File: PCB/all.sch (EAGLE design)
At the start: 41 parts, among them J1 ISP Programmer, U1 ATMEGA32U4, U2 3.3V_REG, U3 MPU-6050-1, U5 MCP73831, U6 AL8805, X1 USBSMD

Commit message: Still playing with GIT - this time I wanted to see how does it recognize the changes in Eagle files.
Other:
- note added: "Tie AD0 somewhere! (to pin 8 is the best) Otherwise, the chip won't work!"
- note removed: "Tie AD0 somewhere! (to pin 8 is the best)"
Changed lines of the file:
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@@
 <?xml version="1.0" encoding="utf-8"?>
 <!DOCTYPE eagle SYSTEM "eagle.dtd">
-<eagle version="7.4.0">
+<eagle version="7.3.0">
 <drawing>
 <settings>
@@
 <text x="179.324" y="-13.716" size="3.81" layer="91">for 3.3V, XTAL
 should be max 8MHz!!!</text>
-<text x="355.6" y="-55.88" size="1.778" layer="91">Tie AD0 somewhere!
-(to pin 8 is the best)</text>
+<text x="353.06" y="-60.96" size="1.778" layer="91">Tie AD0 somewhere!
+(to pin 8 is the best)
+Otherwise, the chip won't work!</text>
 </plain>
 <instances>

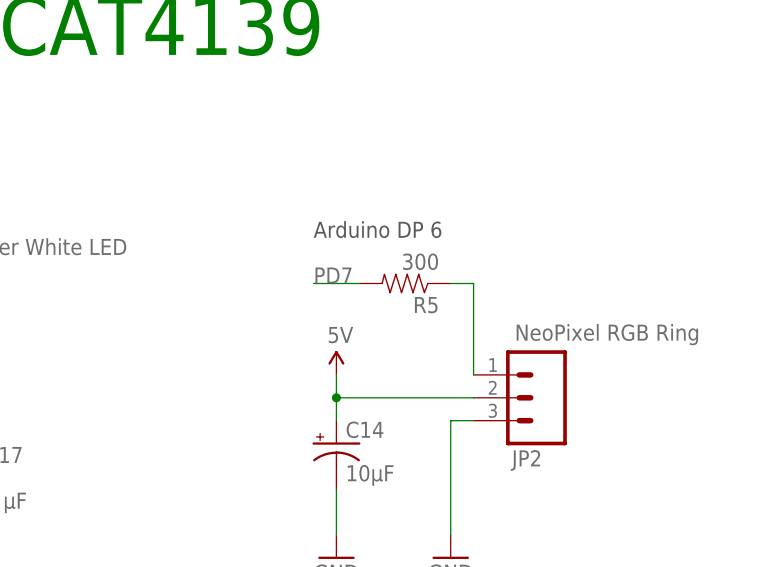
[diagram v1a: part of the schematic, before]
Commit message: added 3D models
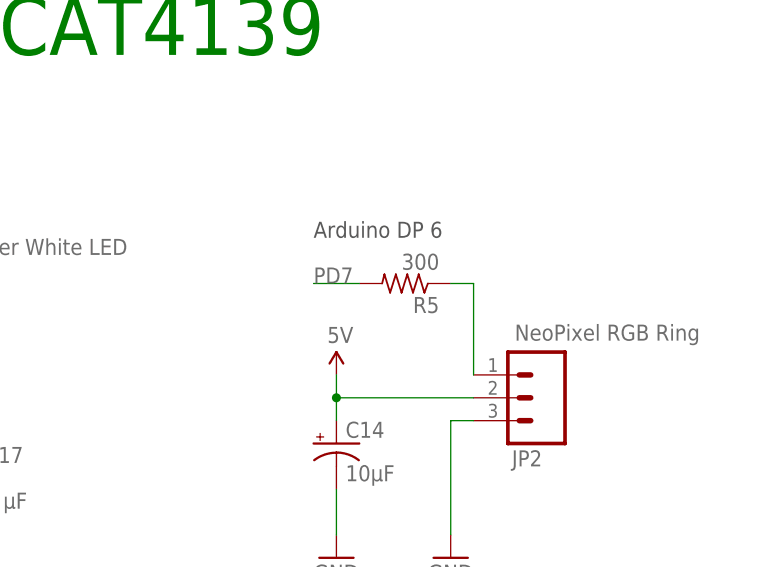
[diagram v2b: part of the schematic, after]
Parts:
- R5: device SparkFun:RESISTOR0603-RES -> rcl:R-US_R0603
- U1: device SparkFun:ATMEGA32U4QFN2 -> SparkFun-Retired:ATMEGA32U4QFN2
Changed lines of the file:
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@@
 <layers>
 <layer number="1" name="Top" color="4" fill="1" visible="no" active="no"/>
+<layer number="2" name="Route2" color="1" fill="3" visible="no" active="no"/>
+<layer number="3" name="Route3" color="4" fill="3" visible="no" active="no"/>
+<layer number="4" name="Route4" color="1" fill="4" visible="no" active="no"/>
+<layer number="5" name="Route5" color="4" fill="4" visible="no" active="no"/>
+<layer number="6" name="Route6" color="1" fill="8" visible="no" active="no"/>
+<layer number="7" name="Route7" color="4" fill="8" visible="no" active="no"/>
+<layer number="8" name="Route8" color="1" fill="2" visible="no" active="no"/>
+<layer number="9" name="Route9" color="4" fill="2" visible="no" active="no"/>
+<layer number="10" name="Route10" color="1" fill="7" visible="no" active="no"/>
+<layer number="11" name="Route11" color="4" fill="7" visible="no" active="no"/>
+<layer number="12" name="Route12" color="1" fill="5" visible="no" active="no"/>
+<layer number="13" name="Route13" color="4" fill="5" visible="no" active="no"/>
+<layer number="14" name="Route14" color="1" fill="6" visible="no" active="no"/>
+<layer number="15" name="Route15" color="4" fill="6" visible="no" active="no"/>
 <layer number="16" name="Bottom" color="1" fill="1" visible="no" active="no"/>
 <layer number="17" name="Pads" color="2" fill="1" visible="no" active="no"/>
@@
 <layer number="54" name="bGND_GNDA" color="1" fill="9" visible="no" active="no"/>
 <layer number="56" name="wert" color="7" fill="1" visible="no" active="no"/>
+<layer number="57" name="tCAD" color="7" fill="1" visible="no" active="no"/>
+<layer number="59" name="tCarbon" color="7" fill="1" visible="no" active="no"/>
+<layer number="60" name="bCarbon" color="7" fill="1" visible="no" active="no"/>
+<layer number="90" name="Modules" color="5" fill="1" visible="yes" active="yes"/>
 <layer number="91" name="Nets" color="2" fill="1" visible="yes" active="yes"/>
 <layer number="92" name="Busses" color="1" fill="1" visible="yes" active="yes"/>
@@
 <layer number="108" name="tplace-old" color="10" fill="1" visible="yes" active="yes"/>
 <layer number="109" name="ref-old" color="11" fill="1" visible="yes" active="yes"/>
+<layer number="110" name="fp0" color="7" fill="1" visible="no" active="yes"/>
+<layer number="111" name="LPC17xx" color="7" fill="1" visible="no" active="yes"/>
+<layer number="112" name="tSilk" color="7" fill="1" visible="no" active="yes"/>
+<layer number="113" name="IDFDebug" color="4" fill="1" visible="no" active="yes"/>
 <layer number="116" name="Patch_BOT" color="9" fill="4" visible="no" active="yes"/>
 <layer number="121" name="_tsilk" color="7" fill="1" visible="no" active="yes"/>
 <layer number="122" name="_bsilk" color="7" fill="1" visible="no" active="yes"/>
+<layer number="123" name="tTestmark" color="7" fill="1" visible="no" active="yes"/>
+<layer number="124" name="bTestmark" color="7" fill="1" visible="no" active="yes"/>
 <layer number="125" name="_tNames" color="7" fill="1" visible="no" active="yes"/>
+<layer number="126" name="_bNames" color="7" fill="1" visible="no" active="yes"/>
+<layer number="127" name="_tValues" color="7" fill="1" visible="no" active="yes"/>
+<layer number="128" name="_bValues" color="7" fill="1" visible="no" active="yes"/>
+<layer number="129" name="Mask" color="7" fill="1" visible="yes" active="yes"/>
+<layer number="131" name="tAdjust" color="7" fill="1" visible="no" active="yes"/>
+<layer number="132" name="bAdjust" color="7" fill="1" visible="no" active="yes"/>
 <layer number="144" name="Drill_legend" color="7" fill="1" visible="no" active="yes"/>
+<layer number="150" name="Notes" color="7" fill="1" visible="no" active="yes"/>
 <layer number="151" name="HeatSink" color="7" fill="1" visible="no" active="yes"/>
+<layer number="152" name="_bDocu" color="7" fill="1" visible="no" active="yes"/>
+<layer number="153" name="FabDoc1" color="7" fill="1" visible="no" active="yes"/>
+<layer number="154" name="FabDoc2" color="7" fill="1" visible="no" active="yes"/>
+<layer number="155" name="FabDoc3" color="7" fill="1" visible="no" active="yes"/>
 <layer number="199" name="Contour" color="7" fill="1" visible="no" active="yes"/>
 <layer number="200" name="200bmp" color="1" fill="10" visible="no" active="yes"/>
@@
 <layer number="223" name="223bmp" color="24" fill="1" visible="no" active="no"/>
 <layer number="224" name="224bmp" color="25" fill="1" visible="no" active="no"/>
+<layer number="225" name="225bmp" color="7" fill="1" visible="yes" active="yes"/>
+<layer number="226" name="226bmp" color="7" fill="1" visible="yes" active="yes"/>
+<layer number="227" name="227bmp" color="7" fill="1" visible="yes" active="yes"/>
+<layer number="228" name="228bmp" color="7" fill="1" visible="yes" active="yes"/>
+<layer number="229" name="229bmp" color="7" fill="1" visible="yes" active="yes"/>
+<layer number="230" name="230bmp" color="7" fill="1" visible="yes" active="yes"/>
+<layer number="231" name="231bmp" color="7" fill="1" visible="yes" active="yes"/>
+<layer number="248" name="Housing" color="7" fill="1" visible="no" active="yes"/>
+<layer number="249" name="Edge" color="7" fill="1" visible="no" active="yes"/>
 <layer number="250" name="Descript" color="3" fill="1" visible="no" active="no"/>
 <layer number="251" name="SMDround" color="12" fill="11" visible="no" active="no"/>
 <layer number="254" name="cooling" color="7" fill="1" visible="no" active="yes"/>
+<layer number="255" name="routoute" color="7" fill="1" visible="yes" active="yes"/>
 </layers>
 <schematic xreflabel="%F%N/%S.%C%R" xrefpart="/%S.%C%R">
@@
 </classes>
 <parts>
-<part name="U1" library="SparkFun" deviceset="ATMEGA32U4" device="QFN2" value="ATMEGA32U4"/>
+<part name="U1" library="SparkFun-Retired" deviceset="ATMEGA32U4" device="QFN2" value="ATMEGA32U4"/>
 <part name="R1" library="rcl" deviceset="R-US_" device="R0603" value="10k"/>
 <part name="C1" library="rcl" deviceset="C-EU" device="C0402" value="0.1μF"/>
@@
 <part name="U$5" library="SparkFun" deviceset="5V" device=""/>
 <part name="GND24" library="SparkFun" deviceset="GND" device=""/>
-<part name="R5" library="SparkFun" deviceset="RESISTOR" device="0603-RES" value="300"/>
+<part name="R5" library="rcl" deviceset="R-US_" device="R0603" value="300"/>
 <part name="C14" library="SparkFun" deviceset="CAP_POL" device="1206" value="10μF"/>
 <part name="GND21" library="SparkFun" deviceset="GND" device=""/>

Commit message: Adding Qi receiver modules
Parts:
- removed F1: PTCSMD, SparkFun:PTCSMD
- removed XTAL1: 16MHz, SparkFun:CRYSTAL5X3
- added C18, C19, C20, C21, C22, C23, C24, C25, C26, C27, C28, C29: 10μF, SparkFun:CAP_POL1206
- added CP1, CP2, CP3, CP4, CP5, CP6, CP7, CP8, CS, CS10, CS17, CS20, CS27, CS30, CS37, CS7: 18pF, rcl:C-EUC0603
- added CS1, CS11, CS12, CS2, CS21, CS22, CS31, CS32: 10nF, rcl:C-EUC0603
- added CS13, CS15, CS23, CS25, CS3, CS33, CS35, CS5: 0.47μF, rcl:C-EUC0603
- added CS14, CS16, CS24, CS26, CS34, CS36, CS4, CS6: 22nF, rcl:C-EUC0603
- added CS18, CS19, CS28, CS29, CS38, CS39, CS8, CS9: 100nF, rcl:C-EUC0603
- added J3, J4, J5, J6: (no value), SparkFun-Connectors:M02PTH2
- added R10, R11, R14, R17: 10k, rcl:R-EU_R0603
- added R12, R15, R4: 188, rcl:R-EU_R0603
- added R13, R16, R9: 230, rcl:R-EU_R0603
- added U4, U7, U8, U9: BQ51013B_RHL_20, pero_library:BQ51013B_RHL_20
- L1: value 33 μH -> 56uH
- R2: value 22 -> 188; device rcl:R-US_R0603 -> rcl:R-EU_R0603
- R3: value 22 -> 230; device rcl:R-US_R0603 -> rcl:R-EU_R0603
- X1: value USBSMD -> 8MHz; device SparkFun:USBSMD -> pero_library:QUARTZ-CRYSTAL-8MHZQC6CB8.00000F18B23R
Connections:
- removed net D+: R2.1, X1.D+
- removed net D-: R3.1, X1.D-
- new net N$10: CS.1, CS7.1, J3.2
- new net N$11: CP1.1, CP2.1, CS2.1, CS3.1, CS4.1, J3.1, U4.AC2
- new net N$12: CS1.2, U4.BOOT1
- new net N$13: CS2.2, U4.BOOT2
- new net N$14: CS3.2, U4.CLMP2
- new net N$19: CS4.2, U4.COM2
- new net N$20: CS6.2, U4.COM1
- new net N$21: CS5.2, U4.CLMP1
- new net N$22: CS12.2, U7.BOOT2
- new net N$23: C20.+, C21.+, CS9.1, U4.RECT
- new net N$24: R9.2, U4.ILIM
- new net N$25: R4.2, R9.1, U4.FOD
- new net N$26: R10.1, U4.TS-CTRL
- new net N$27: CS13.2, U7.CLMP2
- new net N$28: CS14.2, U7.COM2
- new net N$29: CS16.2, U7.COM1
- new net N$30: CS15.2, U7.CLMP1
- new net N$31: CP3.2, CP4.2, CS10.2, CS11.1, CS15.1, CS16.1, CS17.2, U7.AC1
- new net N$32: C22.+, C23.+, CS19.1, U7.RECT
- new net N$33: R3.2, U7.ILIM
- new net N$34: R2.2, R3.1, U7.FOD
- new net N$35: R11.1, U7.TS-CTRL
- new net N$36: CS20.1, CS27.1, J5.2
- new net N$37: CP5.1, CP6.1, CS22.1, CS23.1, CS24.1, J5.1, U8.AC2
- new net N$38: CS21.2, U8.BOOT1
- new net N$39: CS22.2, U8.BOOT2
- new net N$40: CS23.2, U8.CLMP2
- new net N$41: CS24.2, U8.COM2
- new net N$42: CS26.2, U8.COM1
- new net N$43: CS25.2, U8.CLMP1
- new net N$44: CP5.2, CP6.2, CS20.2, CS21.1, CS25.1, CS26.1, CS27.2, U8.AC1
- new net N$45: C25.+, C26.+, CS29.1, U8.RECT
- new net N$46: R13.2, U8.ILIM
- new net N$47: R12.2, R13.1, U8.FOD
- new net N$48: R14.1, U8.TS-CTRL
- new net N$49: CS30.1, CS37.1, J6.2
- new net N$50: CP7.1, CP8.1, CS32.1, CS33.1, CS34.1, J6.1, U9.AC2
- new net N$51: CS31.2, U9.BOOT1
- new net N$52: CS32.2, U9.BOOT2
- new net N$53: CS33.2, U9.CLMP2
- new net N$54: CS34.2, U9.COM2
- new net N$55: CS36.2, U9.COM1
- new net N$56: CS35.2, U9.CLMP1
- new net N$57: CP7.2, CP8.2, CS30.2, CS31.1, CS35.1, CS36.1, CS37.2, U9.AC1
- new net N$58: C28.+, C29.+, CS39.1, U9.RECT
- new net N$59: R16.2, U9.ILIM
- new net N$60: R15.2, R16.1, U9.FOD
- new net N$61: R17.1, U9.TS-CTRL
- new net N$9: CP1.2, CP2.2, CS.2, CS1.1, CS5.1, CS6.1, CS7.2, U4.AC1
- new net V_QI1: C18.+, CS18.1, U7.OUT
- new net V_QI2: C19.+, CS8.1, U4.OUT
- new net V_QI3: C24.+, CS28.1, U8.OUT
- new net V_QI4: C27.+, CS38.1, U9.OUT
- net GND: now also C18.-, C19.-, C20.-, C21.-, C22.-, C23.-, C24.-, C25.-, C26.-, C27.-, C28.-, C29.-, CS18.2, CS19.2, CS28.2, CS29.2, CS38.2, CS39.2, CS8.2, CS9.2, R10.2, R11.2, R12.1, R14.2, R15.1, R17.2, R2.1, R4.1, U4.AD, U4.EN1, U4.EN2, U4.EPAD, U4.PGND, U4.PGND_2, U7.AD, U7.EN1, U7.EN2, U7.EPAD, U7.PGND, U7.PGND_2, U8.AD, U8.EN1, U8.EN2, U8.EPAD, U8.PGND, U8.PGND_2, U9.AD, U9.EN1, U9.EN2, U9.EPAD, U9.PGND, U9.PGND_2; no longer X1.GND
- net N$16: now also CS11.2, U7.BOOT1; no longer F1.1, X1.VBUS
- net N$2: now also X1.2; no longer XTAL1.2
- net N$3: now also X1.1; no longer XTAL1.1
- net N$4: no longer F1.2, U1.UVCC, U1.VBUS
- net N$6: now also CS10.1, CS17.1, J4.2; no longer R2.2, U1.D+
- net N$8: now also CP3.1, CP4.1, CS12.1, CS13.1, CS14.1, J4.1, U7.AC2; no longer R3.2, U1.D-
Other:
- note removed: "for 3.3V, XTAL should be max 8MHz!!!"

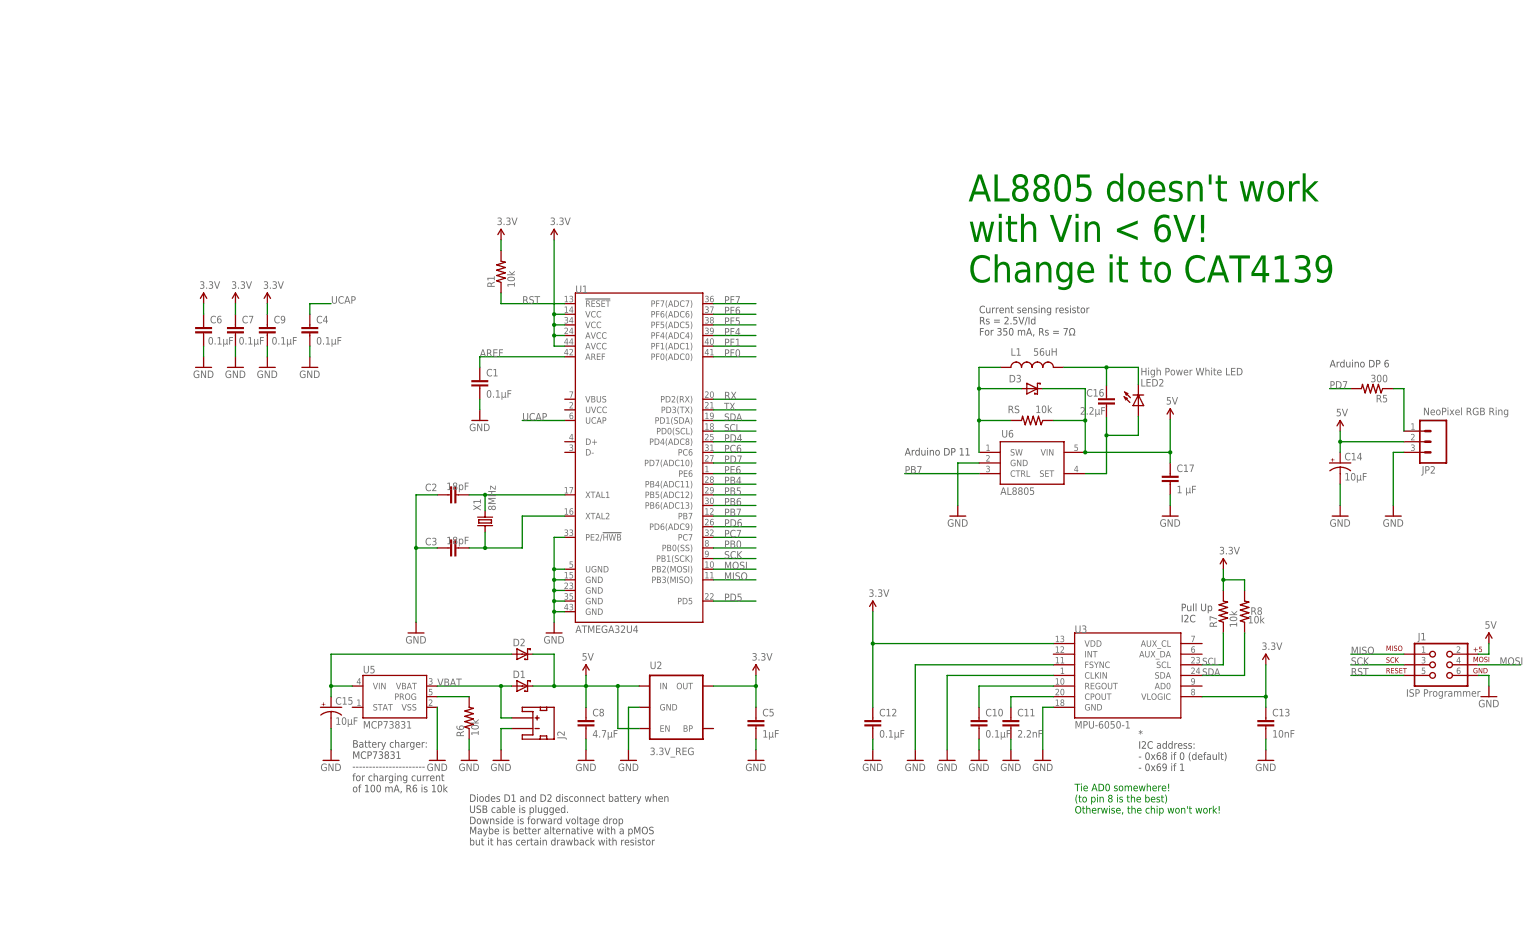
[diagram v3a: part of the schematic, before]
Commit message: Adding Tiny163 4 instead of mega32u4
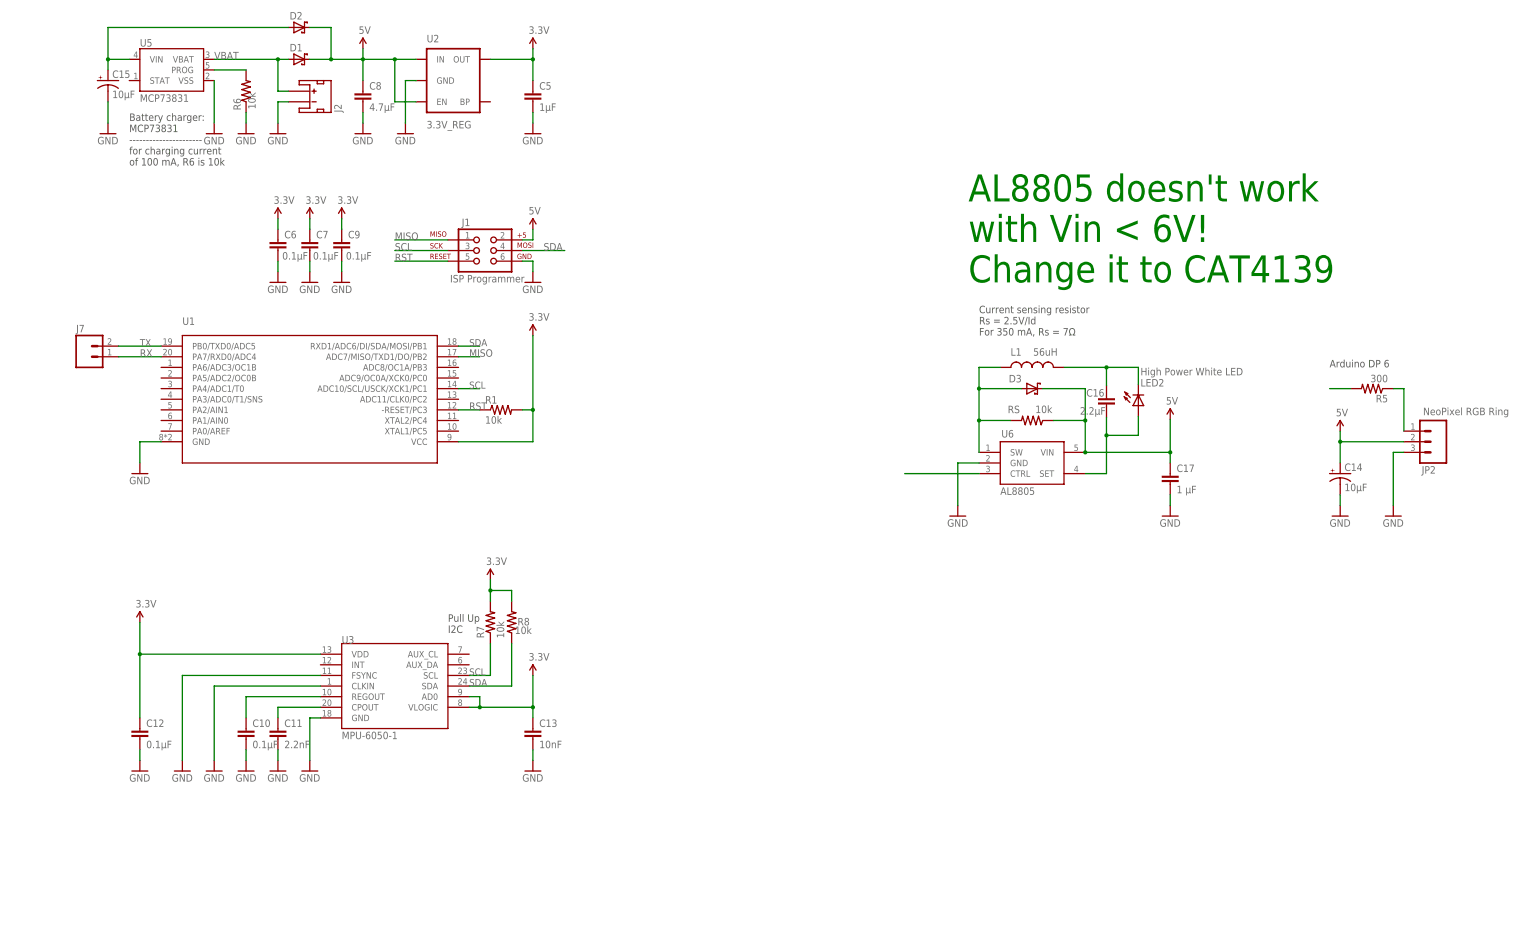
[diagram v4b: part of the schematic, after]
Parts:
- removed C1, C4: 0.1μF, rcl:C-EUC0402
- removed C2, C3: 18pF, rcl:C-EUC0603
- removed X1: 8MHz, pero_library:QUARTZ-CRYSTAL-8MHZQC6CB8.00000F18B23R
- added J7: (no value), SparkFun-Connectors:M02PTH
- U1: value ATMEGA32U4 -> ATTINY1634MLF20; device SparkFun-Retired:ATMEGA32U4QFN2 -> attiny1634:ATTINY1634MLF20
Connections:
- removed net AREF: C1.1, U1.AREF
- removed net MOSI: J1.4, U1.PB2(MOSI)
- removed net N$2: C2.2, U1.XTAL1, X1.2
- removed net N$3: C3.2, U1.XTAL2, X1.1
- removed net PB0: U1.PB0(SS)
- removed net PB4: U1.PB4(ADC11)
- removed net PB5: U1.PB5(ADC12)
- removed net PB6: U1.PB6(ADC13)
- removed net PC6: U1.PC6
- removed net PC7: U1.PC7
- removed net PD4: U1.PD4(ADC8)
- removed net PD5: U1.PD5
- removed net PD6: U1.PD6(ADC9)
- removed net PE6: U1.PE6
- removed net PF0: U1.PF0(ADC0)
- removed net PF1: U1.PF1(ADC1)
- removed net PF4: U1.PF4(ADC4)
- removed net PF5: U1.PF5(ADC5)
- removed net PF6: U1.PF6(ADC6)
- removed net PF7: U1.PF7(ADC7)
- removed net SCK: J1.3, U1.PB1(SCK)
- removed net UCAP: C4.1, U1.UCAP
- net 3.3V: now also U1.VCC, U3.AD0; no longer U1.AVCC@24, U1.AVCC@44, U1.VCC@14, U1.VCC@34
- net GND: now also U1.GND; no longer C1.2, C2.1, C3.1, C4.2, U1.GND@15, U1.GND@23, U1.GND@35, U1.GND@43, U1.PE2/!HWB, U1.UGND
- net MISO: now also U1.ADC7/MISO/TXD1/DO/PB2; no longer U1.PB3(MISO)
- net PB7: no longer U1.PB7
- net PD7: no longer U1.PD7(ADC10)
- net RST: now also U1.-RESET/PC3; no longer U1.!RESET
- net RX: now also J7.1, U1.PA7/RXD0/ADC4; no longer U1.PD2(RX)
- net SCL: now also J1.3, U1.ADC10/SCL/USCK/XCK1/PC1; no longer U1.PD0(SCL)
- net SDA: now also J1.4, U1.RXD1/ADC6/DI/SDA/MOSI/PB1; no longer U1.PD1(SDA)
- net TX: now also J7.2, U1.PB0/TXD0/ADC5; no longer U1.PD3(TX)
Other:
- note removed: "* I2C address: - 0x68 if 0 (default) - 0x69 if 1"
- note removed: "Arduino DP 11"
- note removed: "Diodes D1 and D2 disconnect battery when USB cable is plugged. Downside is forward voltage drop"
- note removed: "Maybe is better alternative with a pMOS but it has certain drawback with resistor"
- note removed: "Tie AD0 somewhere! (to pin 8 is the best) Otherwise, the chip won't work!"
- moved on the sheet: C10, C11, C12, C13, C14, C15, C5, C6, C7, C8, C9, D1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

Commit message: Two-sheet schematics, and routing Qi chargers
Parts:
- removed LED2: High Power White LED, led:LED5MM
- added D4, D5, D6: SMF5.0AT1, diode:SMF5.0AT1
- added J8: BL-HP20AUW2C, SparkFun-Connectors:M02PTH
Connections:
- removed net N$4: C15.+, D2.A, U5.VIN
- removed net PB7: U6.CTRL
- removed net PD7: R5.2
- new net PWM: U1.ADC9/OC0A/XCK0/PC0, U6.CTRL
- new net RGB: R5.2, U1.PA6/ADC3/OC1B
- new net V_QI_IN: C15.+, D2.C, D4.C, D5.C, D6.C, U5.VIN
- net 5V: no longer D2.C
- net ANODE: no longer LED2.A
- net CATHODE: no longer LED2.C
- net V_QI1: now also D2.A
- net V_QI2: now also D4.A
- net V_QI3: now also D5.A
- net V_QI4: now also D6.A
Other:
- note added: "Loveread Lamp Version 2.0 Pero 2016"
- note added: "Main circuit"
- note added: "Qi chargers"
- note removed: "Arduino DP 6"
- note removed: "Loveread Lamp Version 1.0 Pero 2015"
- note removed: "Pull Up I2C"
